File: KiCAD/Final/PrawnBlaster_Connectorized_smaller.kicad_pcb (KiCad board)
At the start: 2 copper layers, 93 x 58.4 mm, 37 parts, among them IC1 74LVT245D,118, J1 PWR SEL, J2 Ext. Clock, J3 Ext. Trig., J4 Pseudoclock 3, J5 Pseudoclock 1, J6 Pseudoclock 2, J7 Pseudoclock 0, J8 EXT PWR, U2 74LVC1G34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

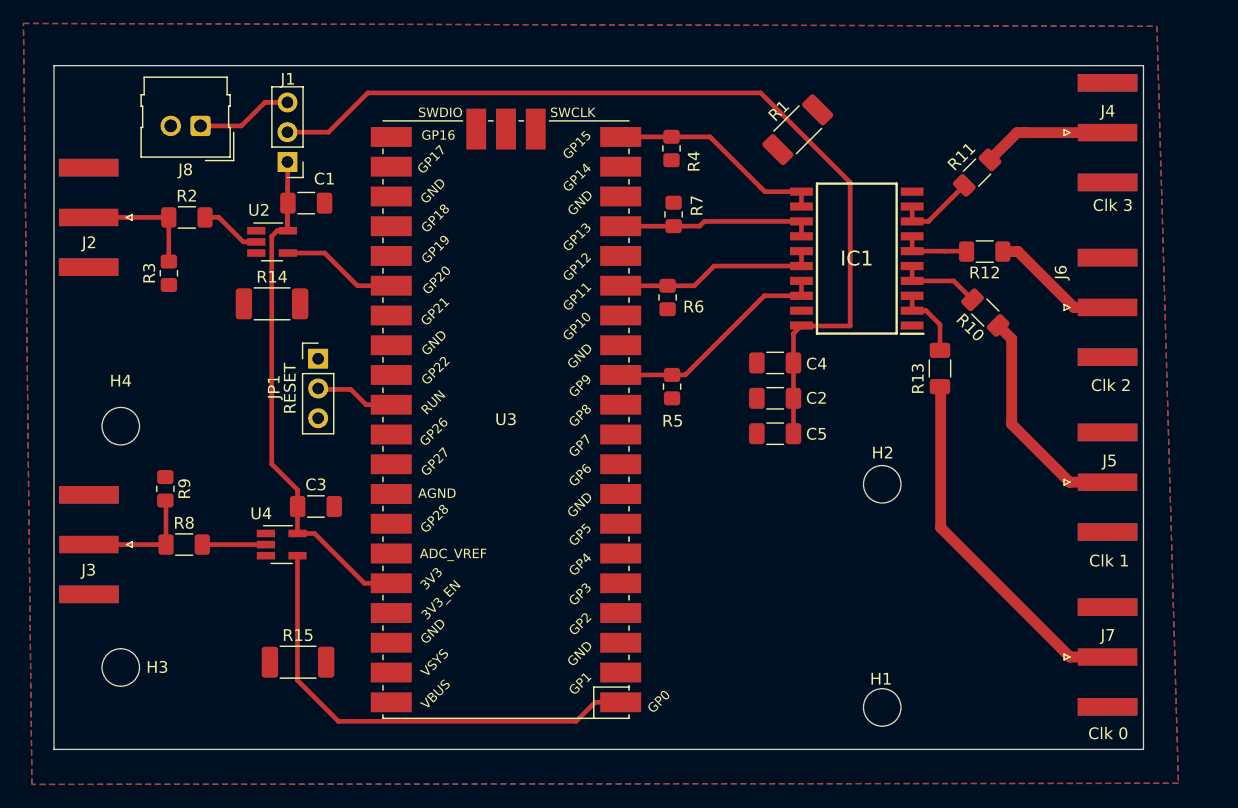
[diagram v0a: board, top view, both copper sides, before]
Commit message: Revert "Push through"
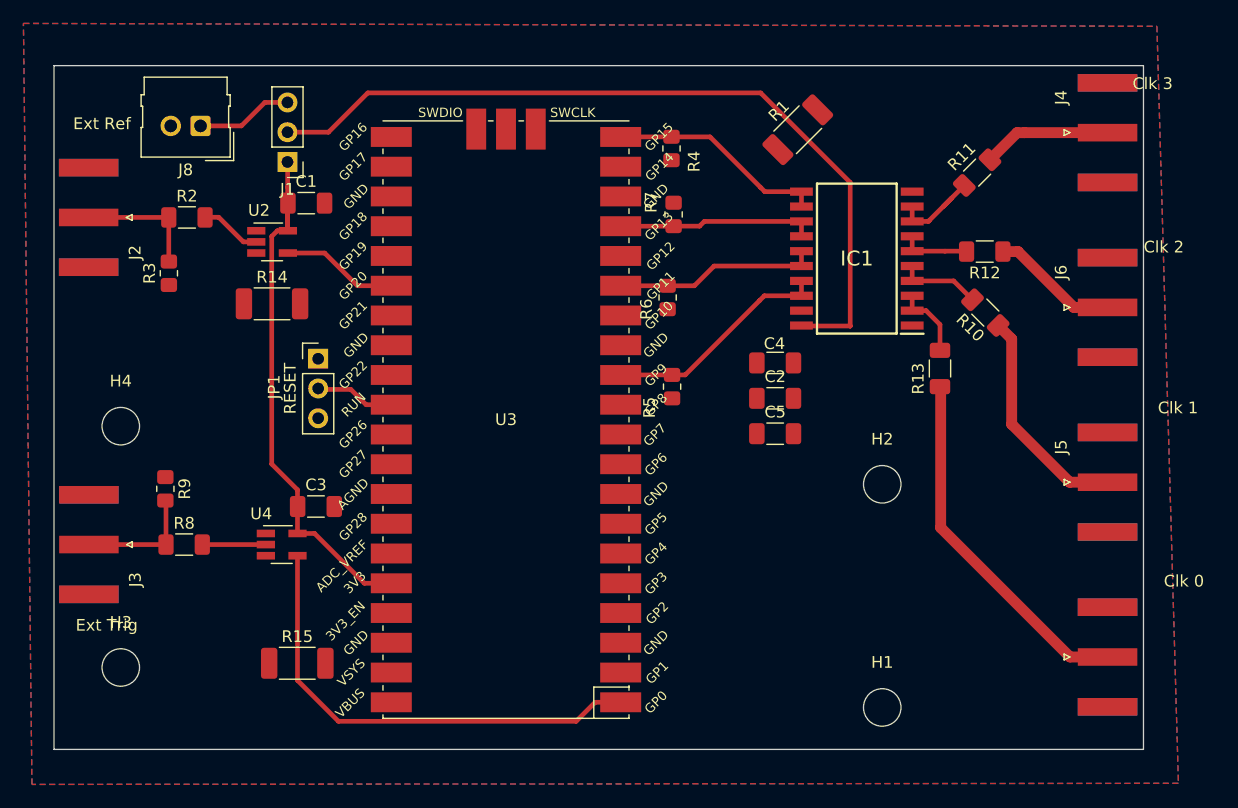
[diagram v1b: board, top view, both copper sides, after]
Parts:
- moved R15 0.11 mm to (107.8, 108.2)
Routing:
- net Power Supply: track 78.5 -> 69.0 mm
- net Net-(IC1-A6): track 7.00 -> 8.03 mm
